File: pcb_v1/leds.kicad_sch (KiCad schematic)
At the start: 66 parts

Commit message: Included Capacitors and JST connector in schematic. Upgraded MC to 69 pin version
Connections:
- net PWRG: now also LED21.1 (GK), LED22.1 (GK); no longer LED1.2 (RK), LED10.2 (RK), LED11.2 (RK), LED12.2 (RK), LED13.2 (RK), LED14.2 (RK), LED15.2 (RK), LED17.2 (RK), LED18.2 (RK), LED19.2 (RK), LED2.2 (RK), LED20.2 (RK), LED21.2 (RK), LED22.2 (RK), LED23.2 (RK), LED24.2 (RK), LED25.2 (RK), LED26.2 (RK), LED27.2 (RK), LED28.2 (RK), LED29.2 (RK), LED30.2 (RK), LED31.2 (RK), LED32.2 (RK), LED33.2 (RK), LED34.2 (RK), LED35.2 (RK), LED36.2 (RK), LED37.2 (RK), LED38.2 (RK), LED39.2 (RK), LED40.2 (RK), LED41.2 (RK), LED42.2 (RK), LED43.2 (RK), LED44.2 (RK), LED45.2 (RK), LED46.2 (RK), LED47.2 (RK), LED48.2 (RK), LED49.2 (RK), LED5.2 (RK), LED50.2 (RK), LED51.2 (RK), LED52.2 (RK), LED53.2 (RK), LED54.2 (RK), LED55.2 (RK), LED56.2 (RK), LED57.2 (RK), LED58.2 (RK), LED59.2 (RK), LED6.2 (RK), LED60.2 (RK), LED62.2 (RK), LED64.2 (RK), LED65.2 (RK), LED66.2 (RK), LED7.2 (RK), LED8.2 (RK), LED9.2 (RK)
- net PWRR: now reaches LED3.2 (RK)
- net PWRR: now also LED1.2 (RK), LED10.2 (RK), LED11.2 (RK), LED12.2 (RK), LED13.2 (RK), LED14.2 (RK), LED15.2 (RK), LED16.2 (RK), LED17.2 (RK), LED18.2 (RK), LED19.2 (RK), LED2.2 (RK), LED20.2 (RK), LED21.2 (RK), LED22.2 (RK), LED23.2 (RK), LED24.2 (RK), LED25.2 (RK), LED26.2 (RK), LED27.2 (RK), LED28.2 (RK), LED29.2 (RK), LED30.2 (RK), LED31.2 (RK), LED32.2 (RK), LED33.2 (RK), LED34.2 (RK), LED35.2 (RK), LED36.2 (RK), LED37.2 (RK), LED38.2 (RK), LED39.2 (RK), LED4.2 (RK), LED40.2 (RK), LED41.2 (RK), LED42.2 (RK), LED43.2 (RK), LED44.2 (RK), LED45.2 (RK), LED46.2 (RK), LED47.2 (RK), LED48.2 (RK), LED49.2 (RK), LED5.2 (RK), LED50.2 (RK), LED51.2 (RK), LED52.2 (RK), LED53.2 (RK), LED54.2 (RK), LED55.2 (RK), LED56.2 (RK), LED57.2 (RK), LED58.2 (RK), LED59.2 (RK), LED6.2 (RK), LED60.2 (RK), LED61.2 (RK), LED62.2 (RK), LED64.2 (RK), LED65.2 (RK), LED66.2 (RK), LED7.2 (RK), LED8.2 (RK), LED9.2 (RK)

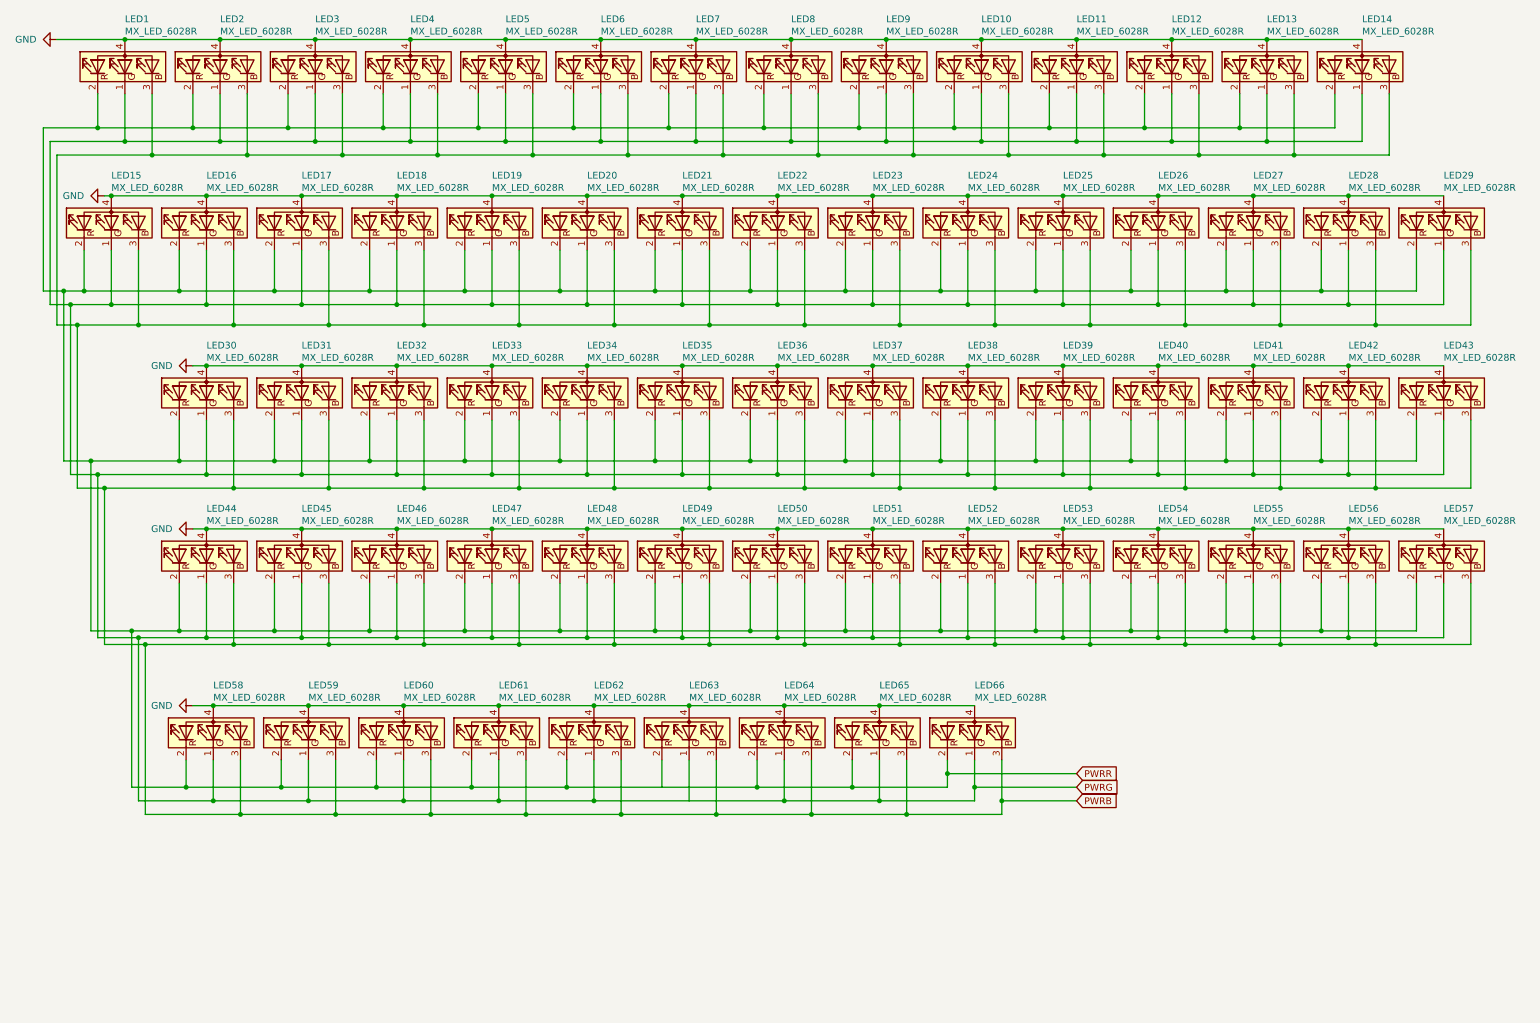
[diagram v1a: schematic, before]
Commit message: New LED Schematic
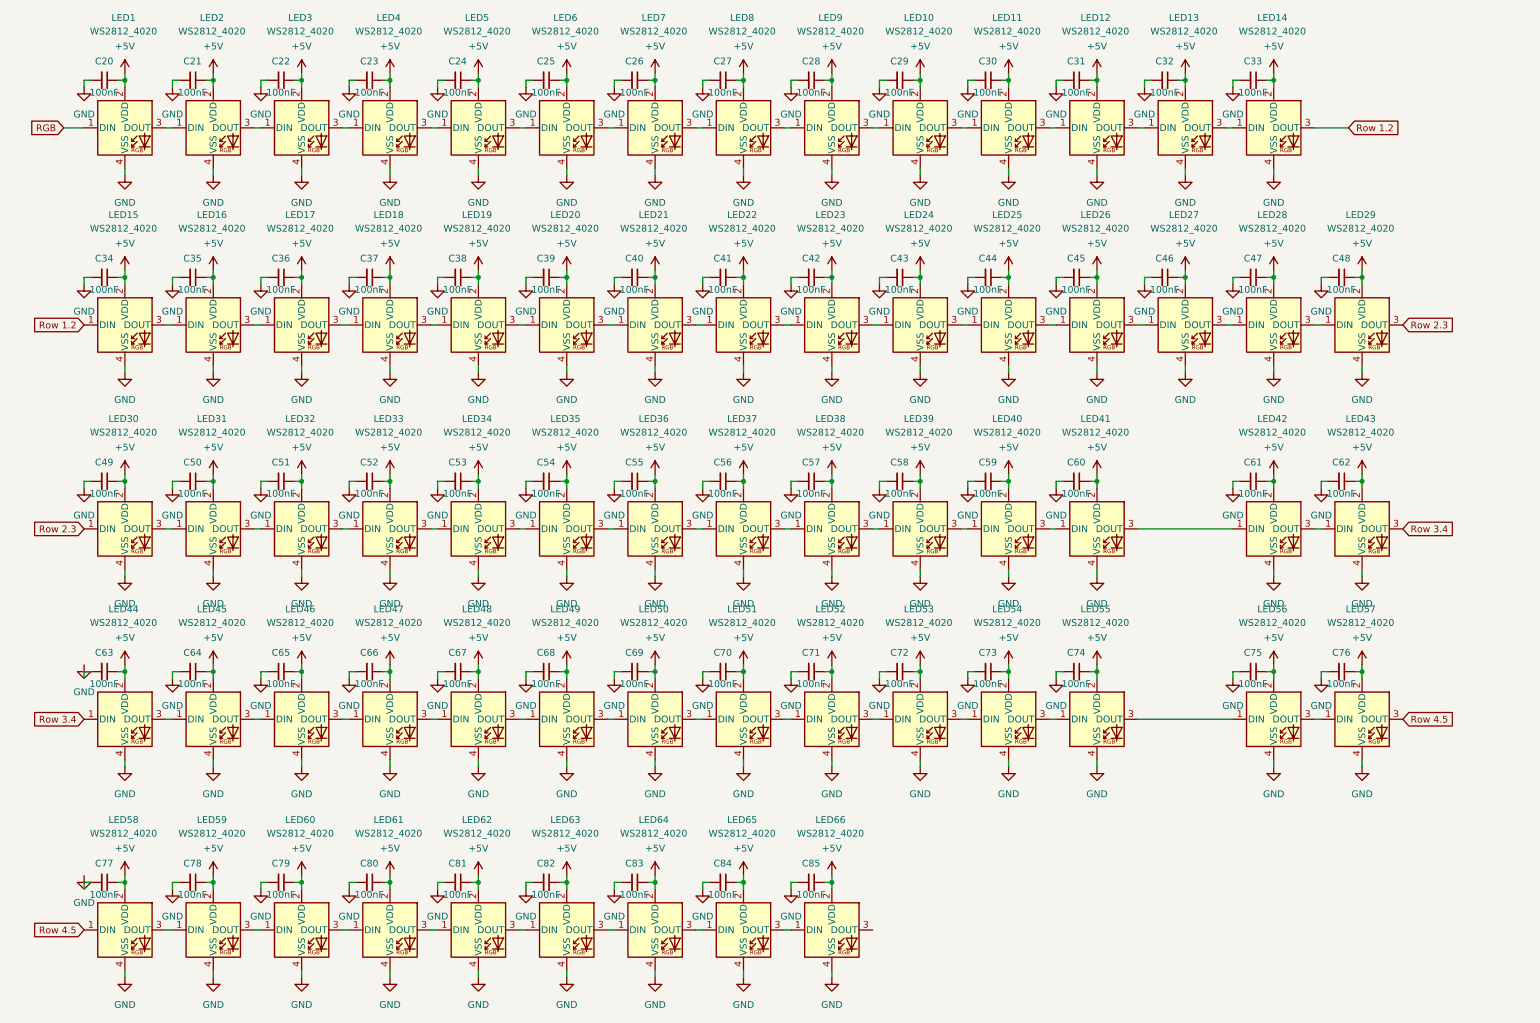
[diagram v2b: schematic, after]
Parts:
- removed LED1, LED10, LED11, LED12, LED13, LED14, LED15, LED16, LED17, LED18, LED19, LED2, LED20, LED21, LED22, LED23, LED24, LED25, LED26, LED27, LED28, LED29, LED3, LED30, LED31, LED32, LED33, LED34, LED35, LED36, LED37, LED38, LED39, LED4, LED40, LED41, LED42, LED43, LED44, LED45, LED46, LED47, LED48, LED49, LED5, LED50, LED51, LED52, LED53, LED54, LED55, LED56, LED57, LED58, LED59, LED6, LED60, LED61, LED62, LED63, LED64, LED65, LED66, LED7, LED8, LED9: MX_LED_6028R, PCM_marbastlib-mx:LED_MX_6028R, symbol PCM_marbastlib-mx:MX_LED_6028R
- added C20, C21, C22, C23, C24, C25, C26, C27, C28, C29, C30, C31, C32, C33, C34, C35, C36, C37, C38, C39, C40, C41, C42, C43, C44, C45, C46, C47, C48, C49, C50, C51, C52, C53, C54, C55, C56, C57, C58, C59, C60, C61, C62, C63, C64, C65, C66, C67, C68, C69, C70, C71, C72, C73, C74, C75, C76, C77, C78, C79, C80, C81, C82, C83, C84, C85: 100nF, Capacitor_SMD:C_0805_2012Metric, symbol Device:C_Small
- added LED1, LED10, LED11, LED12, LED13, LED14, LED15, LED16, LED17, LED18, LED19, LED2, LED20, LED21, LED22, LED23, LED24, LED25, LED26, LED27, LED28, LED29, LED3, LED30, LED31, LED32, LED33, LED34, LED35, LED36, LED37, LED38, LED39, LED4, LED40, LED41, LED42, LED43, LED44, LED45, LED46, LED47, LED48, LED49, LED5, LED50, LED51, LED52, LED53, LED54, LED55, LED56, LED57, LED58, LED59, LED6, LED60, LED61, LED62, LED63, LED64, LED65, LED66, LED7, LED8, LED9: WS2812_4020, PCM_marbastlib-various:LED_WS2812_4020, symbol PCM_marbastlib-various:WS2812_4020
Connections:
- net GND: now also C20.2, C21.2, C22.2, C23.2, C24.2, C25.2, C26.2, C27.2, C28.2, C29.2, C30.2, C31.2, C32.2, C33.2, C34.2, C35.2, C36.2, C37.2, C38.2, C39.2, C40.2, C41.2, C42.2, C43.2, C44.2, C45.2, C46.2, C47.2, C48.2, C49.2, C50.2, C51.2, C52.2, C53.2, C54.2, C55.2, C56.2, C57.2, C58.2, C59.2, C60.2, C61.2, C62.2, C64.2, C65.2, C66.2, C67.2, C68.2, C69.2, C70.2, C71.2, C72.2, C73.2, C74.2, C75.2, C76.2, C78.2, C79.2, C80.2, C81.2, C82.2, C83.2, C84.2, C85.2, LED1.4 (VSS), LED10.4 (VSS), LED11.4 (VSS), LED12.4 (VSS), LED13.4 (VSS), LED14.4 (VSS), LED15.4 (VSS), LED16.4 (VSS), LED17.4 (VSS), LED18.4 (VSS), LED19.4 (VSS), LED2.4 (VSS), LED20.4 (VSS), LED21.4 (VSS), LED22.4 (VSS), LED23.4 (VSS), LED24.4 (VSS), LED25.4 (VSS), LED26.4 (VSS), LED27.4 (VSS), LED28.4 (VSS), LED29.4 (VSS), LED3.4 (VSS), LED30.4 (VSS), LED31.4 (VSS), LED32.4 (VSS), LED33.4 (VSS), LED34.4 (VSS), LED35.4 (VSS), LED36.4 (VSS), LED37.4 (VSS), LED38.4 (VSS), LED39.4 (VSS), LED4.4 (VSS), LED40.4 (VSS), LED41.4 (VSS), LED42.4 (VSS), LED43.4 (VSS), LED44.4 (VSS), LED45.4 (VSS), LED46.4 (VSS), LED47.4 (VSS), LED48.4 (VSS), LED49.4 (VSS), LED5.4 (VSS), LED50.4 (VSS), LED51.4 (VSS), LED52.4 (VSS), LED53.4 (VSS), LED54.4 (VSS), LED55.4 (VSS), LED56.4 (VSS), LED57.4 (VSS), LED58.4 (VSS), LED59.4 (VSS), LED6.4 (VSS), LED60.4 (VSS), LED61.4 (VSS), LED62.4 (VSS), LED63.4 (VSS), LED64.4 (VSS), LED65.4 (VSS), LED66.4 (VSS), LED7.4 (VSS), LED8.4 (VSS), LED9.4 (VSS)
- new net: LED1.3 (DOUT), LED2.1 (DIN)
- new net: LED2.3 (DOUT), LED3.1 (DIN)
- new net: LED41.3 (DOUT), LED42.1 (DIN)
- new net: LED42.3 (DOUT), LED43.1 (DIN)
- new net: LED24.3 (DOUT), LED25.1 (DIN)
- new net: LED25.3 (DOUT), LED26.1 (DIN)
- new net: LED21.3 (DOUT), LED22.1 (DIN)
- new net: LED22.3 (DOUT), LED23.1 (DIN)
- new net: LED31.3 (DOUT), LED32.1 (DIN)
- new net: LED32.3 (DOUT), LED33.1 (DIN)
- new net: LED15.3 (DOUT), LED16.1 (DIN)
- new net: LED60.3 (DOUT), LED61.1 (DIN)
- new net: LED61.3 (DOUT), LED62.1 (DIN)
- new net: LED27.3 (DOUT), LED28.1 (DIN)
- new net: LED28.3 (DOUT), LED29.1 (DIN)
- new net: LED49.3 (DOUT), LED50.1 (DIN)
- new net: LED50.3 (DOUT), LED51.1 (DIN)
- new net: LED4.3 (DOUT), LED5.1 (DIN)
- new net: LED5.3 (DOUT), LED6.1 (DIN)
- new net: LED23.3 (DOUT), LED24.1 (DIN)
- new net: LED8.3 (DOUT), LED9.1 (DIN)
- new net: LED10.1 (DIN), LED9.3 (DOUT)
- new net: LED26.3 (DOUT), LED27.1 (DIN)
- new net: LED36.3 (DOUT), LED37.1 (DIN)
- new net: LED37.3 (DOUT), LED38.1 (DIN)
- new net: LED54.3 (DOUT), LED55.1 (DIN)
- new net: LED55.3 (DOUT), LED56.1 (DIN)
- new net: LED16.3 (DOUT), LED17.1 (DIN)
- new net: LED17.3 (DOUT), LED18.1 (DIN)
- new net: LED33.3 (DOUT), LED34.1 (DIN)
- new net: LED34.3 (DOUT), LED35.1 (DIN)
- new net: LED12.3 (DOUT), LED13.1 (DIN)
- new net: LED13.3 (DOUT), LED14.1 (DIN)
- new net: LED3.3 (DOUT), LED4.1 (DIN)
- new net: LED59.3 (DOUT), LED60.1 (DIN)
- new net: LED39.3 (DOUT), LED40.1 (DIN)
- new net: LED40.3 (DOUT), LED41.1 (DIN)
- new net: LED51.3 (DOUT), LED52.1 (DIN)
- new net: LED30.3 (DOUT), LED31.1 (DIN)
- new net: LED6.3 (DOUT), LED7.1 (DIN)
- new net: LED10.3 (DOUT), LED11.1 (DIN)
- new net: LED19.3 (DOUT), LED20.1 (DIN)
- new net: LED20.3 (DOUT), LED21.1 (DIN)
- new net: LED65.3 (DOUT), LED66.1 (DIN)
- new net: LED38.3 (DOUT), LED39.1 (DIN)
- new net: LED56.3 (DOUT), LED57.1 (DIN)
- new net: LED46.3 (DOUT), LED47.1 (DIN)
- new net: LED47.3 (DOUT), LED48.1 (DIN)
- new net: LED48.3 (DOUT), LED49.1 (DIN)
- new net: LED11.3 (DOUT), LED12.1 (DIN)
- new net: LED18.3 (DOUT), LED19.1 (DIN)
- new net: LED44.3 (DOUT), LED45.1 (DIN)
- new net: LED45.3 (DOUT), LED46.1 (DIN)
- new net: LED35.3 (DOUT), LED36.1 (DIN)
- new net: LED63.3 (DOUT), LED64.1 (DIN)
- new net: LED64.3 (DOUT), LED65.1 (DIN)
- new net: LED53.3 (DOUT), LED54.1 (DIN)
- new net: LED62.3 (DOUT), LED63.1 (DIN)
- new net: LED7.3 (DOUT), LED8.1 (DIN)
- new net: LED58.3 (DOUT), LED59.1 (DIN)
- new net: LED52.3 (DOUT), LED53.1 (DIN)
- new net +5V: C20.1, C21.1, C22.1, C23.1, C24.1, C25.1, C26.1, C27.1, C28.1, C29.1, C30.1, C31.1, C32.1, C33.1, C34.1, C35.1, C36.1, C37.1, C38.1, C39.1, C40.1, C41.1, C42.1, C43.1, C44.1, C45.1, C46.1, C47.1, C48.1, C49.1, C50.1, C51.1, C52.1, C53.1, C54.1, C55.1, C56.1, C57.1, C58.1, C59.1, C60.1, C61.1, C62.1, C63.1, C64.1, C65.1, C66.1, C67.1, C68.1, C69.1, C70.1, C71.1, C72.1, C73.1, C74.1, C75.1, C76.1, C77.1, C78.1, C79.1, C80.1, C81.1, C82.1, C83.1, C84.1, C85.1, LED1.2 (VDD), LED10.2 (VDD), LED11.2 (VDD), LED12.2 (VDD), LED13.2 (VDD), LED14.2 (VDD), LED15.2 (VDD), LED16.2 (VDD), LED17.2 (VDD), LED18.2 (VDD), LED19.2 (VDD), LED2.2 (VDD), LED20.2 (VDD), LED21.2 (VDD), LED22.2 (VDD), LED23.2 (VDD), LED24.2 (VDD), LED25.2 (VDD), LED26.2 (VDD), LED27.2 (VDD), LED28.2 (VDD), LED29.2 (VDD), LED3.2 (VDD), LED30.2 (VDD), LED31.2 (VDD), LED32.2 (VDD), LED33.2 (VDD), LED34.2 (VDD), LED35.2 (VDD), LED36.2 (VDD), LED37.2 (VDD), LED38.2 (VDD), LED39.2 (VDD), LED4.2 (VDD), LED40.2 (VDD), LED41.2 (VDD), LED42.2 (VDD), LED43.2 (VDD), LED44.2 (VDD), LED45.2 (VDD), LED46.2 (VDD), LED47.2 (VDD), LED48.2 (VDD), LED49.2 (VDD), LED5.2 (VDD), LED50.2 (VDD), LED51.2 (VDD), LED52.2 (VDD), LED53.2 (VDD), LED54.2 (VDD), LED55.2 (VDD), LED56.2 (VDD), LED57.2 (VDD), LED58.2 (VDD), LED59.2 (VDD), LED6.2 (VDD), LED60.2 (VDD), LED61.2 (VDD), LED62.2 (VDD), LED63.2 (VDD), LED64.2 (VDD), LED65.2 (VDD), LED66.2 (VDD), LED7.2 (VDD), LED8.2 (VDD), LED9.2 (VDD)
- new net RGB: LED1.1 (DIN)
- new net Row 1.2: LED14.3 (DOUT), LED15.1 (DIN)
- new net Row 2.3: LED29.3 (DOUT), LED30.1 (DIN)
- new net Row 3.4: LED43.3 (DOUT), LED44.1 (DIN)
- new net Row 4.5: LED57.3 (DOUT), LED58.1 (DIN)

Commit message: Replaced and wired LEDs and Capacitors
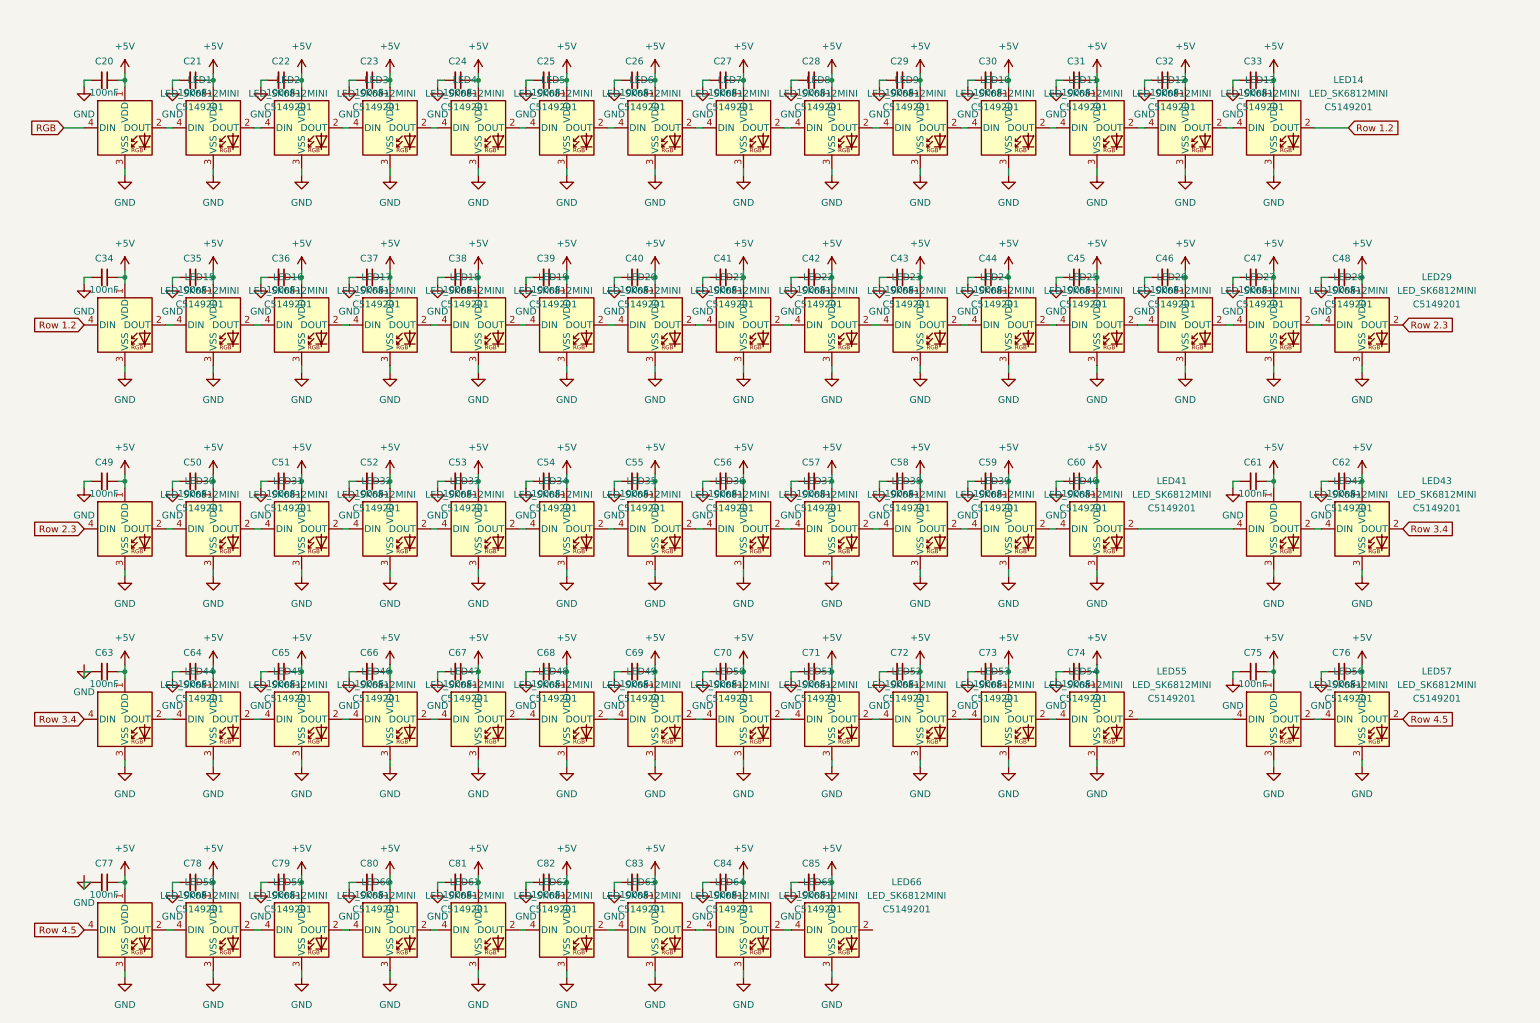
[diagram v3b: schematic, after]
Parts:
- removed LED1, LED10, LED11, LED12, LED13, LED14, LED15, LED16, LED17, LED18, LED19, LED2, LED20, LED21, LED22, LED23, LED24, LED25, LED26, LED27, LED28, LED29, LED3, LED30, LED31, LED32, LED33, LED34, LED35, LED36, LED37, LED38, LED39, LED4, LED40, LED41, LED42, LED43, LED44, LED45, LED46, LED47, LED48, LED49, LED5, LED50, LED51, LED52, LED53, LED54, LED55, LED56, LED57, LED58, LED59, LED6, LED60, LED61, LED62, LED63, LED64, LED65, LED66, LED7, LED8, LED9: WS2812_4020, PCM_marbastlib-various:LED_WS2812_4020, symbol PCM_marbastlib-various:WS2812_4020
- added LED1, LED10, LED11, LED12, LED13, LED14, LED15, LED16, LED17, LED18, LED19, LED2, LED20, LED21, LED22, LED23, LED24, LED25, LED26, LED27, LED28, LED29, LED3, LED30, LED31, LED32, LED33, LED34, LED35, LED36, LED37, LED38, LED39, LED4, LED40, LED41, LED42, LED43, LED44, LED45, LED46, LED47, LED48, LED49, LED5, LED50, LED51, LED52, LED53, LED54, LED55, LED56, LED57, LED58, LED59, LED6, LED60, LED61, LED62, LED63, LED64, LED65, LED66, LED7, LED8, LED9: LED_SK6812MINI, ScottoKeebs_Components:LED_SK6812MINI, symbol ScottoKeebs:LED_SK6812MINI
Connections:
- net +5V: now also LED1.1 (VDD), LED10.1 (VDD), LED11.1 (VDD), LED12.1 (VDD), LED13.1 (VDD), LED14.1 (VDD), LED15.1 (VDD), LED16.1 (VDD), LED17.1 (VDD), LED18.1 (VDD), LED19.1 (VDD), LED2.1 (VDD), LED20.1 (VDD), LED21.1 (VDD), LED22.1 (VDD), LED23.1 (VDD), LED24.1 (VDD), LED25.1 (VDD), LED26.1 (VDD), LED27.1 (VDD), LED28.1 (VDD), LED29.1 (VDD), LED3.1 (VDD), LED30.1 (VDD), LED31.1 (VDD), LED32.1 (VDD), LED33.1 (VDD), LED34.1 (VDD), LED35.1 (VDD), LED36.1 (VDD), LED37.1 (VDD), LED38.1 (VDD), LED39.1 (VDD), LED4.1 (VDD), LED40.1 (VDD), LED41.1 (VDD), LED42.1 (VDD), LED43.1 (VDD), LED44.1 (VDD), LED45.1 (VDD), LED46.1 (VDD), LED47.1 (VDD), LED48.1 (VDD), LED49.1 (VDD), LED5.1 (VDD), LED50.1 (VDD), LED51.1 (VDD), LED52.1 (VDD), LED53.1 (VDD), LED54.1 (VDD), LED55.1 (VDD), LED56.1 (VDD), LED57.1 (VDD), LED58.1 (VDD), LED59.1 (VDD), LED6.1 (VDD), LED60.1 (VDD), LED61.1 (VDD), LED62.1 (VDD), LED63.1 (VDD), LED64.1 (VDD), LED65.1 (VDD), LED66.1 (VDD), LED7.1 (VDD), LED8.1 (VDD), LED9.1 (VDD)
- net GND: now also LED1.3 (VSS), LED10.3 (VSS), LED11.3 (VSS), LED12.3 (VSS), LED13.3 (VSS), LED14.3 (VSS), LED15.3 (VSS), LED16.3 (VSS), LED17.3 (VSS), LED18.3 (VSS), LED19.3 (VSS), LED2.3 (VSS), LED20.3 (VSS), LED21.3 (VSS), LED22.3 (VSS), LED23.3 (VSS), LED24.3 (VSS), LED25.3 (VSS), LED26.3 (VSS), LED27.3 (VSS), LED28.3 (VSS), LED29.3 (VSS), LED3.3 (VSS), LED30.3 (VSS), LED31.3 (VSS), LED32.3 (VSS), LED33.3 (VSS), LED34.3 (VSS), LED35.3 (VSS), LED36.3 (VSS), LED37.3 (VSS), LED38.3 (VSS), LED39.3 (VSS), LED4.3 (VSS), LED40.3 (VSS), LED41.3 (VSS), LED42.3 (VSS), LED43.3 (VSS), LED44.3 (VSS), LED45.3 (VSS), LED46.3 (VSS), LED47.3 (VSS), LED48.3 (VSS), LED49.3 (VSS), LED5.3 (VSS), LED50.3 (VSS), LED51.3 (VSS), LED52.3 (VSS), LED53.3 (VSS), LED54.3 (VSS), LED55.3 (VSS), LED56.3 (VSS), LED57.3 (VSS), LED58.3 (VSS), LED59.3 (VSS), LED6.3 (VSS), LED60.3 (VSS), LED61.3 (VSS), LED62.3 (VSS), LED63.3 (VSS), LED64.3 (VSS), LED65.3 (VSS), LED66.3 (VSS), LED7.3 (VSS), LED8.3 (VSS), LED9.3 (VSS)
- net RGB: now also LED1.4 (DIN)
- net Row 1.2: now also LED14.2 (DOUT), LED15.4 (DIN)
- net Row 2.3: now also LED29.2 (DOUT), LED30.4 (DIN)
- net Row 3.4: now also LED43.2 (DOUT), LED44.4 (DIN)
- net Row 4.5: now also LED57.2 (DOUT), LED58.4 (DIN)
- new net: LED10.4 (DIN), LED9.2 (DOUT)
- new net: LED8.2 (DOUT), LED9.4 (DIN)
- new net: LED42.2 (DOUT), LED43.4 (DIN)
- new net: LED52.2 (DOUT), LED53.4 (DIN)
- new net: LED51.2 (DOUT), LED52.4 (DIN)
- new net: LED19.2 (DOUT), LED20.4 (DIN)
- new net: LED18.2 (DOUT), LED19.4 (DIN)
- new net: LED60.2 (DOUT), LED61.4 (DIN)
- new net: LED59.2 (DOUT), LED60.4 (DIN)
- new net: LED16.2 (DOUT), LED17.4 (DIN)
- new net: LED15.2 (DOUT), LED16.4 (DIN)
- new net: LED3.2 (DOUT), LED4.4 (DIN)
- new net: LED2.2 (DOUT), LED3.4 (DIN)
- new net: LED61.2 (DOUT), LED62.4 (DIN)
- new net: LED65.2 (DOUT), LED66.4 (DIN)
- new net: LED22.2 (DOUT), LED23.4 (DIN)
- new net: LED21.2 (DOUT), LED22.4 (DIN)
- new net: LED50.2 (DOUT), LED51.4 (DIN)
- new net: LED49.2 (DOUT), LED50.4 (DIN)
- new net: LED27.2 (DOUT), LED28.4 (DIN)
- new net: LED26.2 (DOUT), LED27.4 (DIN)
- new net: LED34.2 (DOUT), LED35.4 (DIN)
- new net: LED33.2 (DOUT), LED34.4 (DIN)
- new net: LED64.2 (DOUT), LED65.4 (DIN)
- new net: LED63.2 (DOUT), LED64.4 (DIN)
- new net: LED28.2 (DOUT), LED29.4 (DIN)
- new net: LED7.2 (DOUT), LED8.4 (DIN)
- new net: LED6.2 (DOUT), LED7.4 (DIN)
- new net: LED5.2 (DOUT), LED6.4 (DIN)
- new net: LED4.2 (DOUT), LED5.4 (DIN)
- new net: LED38.2 (DOUT), LED39.4 (DIN)
- new net: LED37.2 (DOUT), LED38.4 (DIN)
- new net: LED1.2 (DOUT), LED2.4 (DIN)
- new net: LED13.2 (DOUT), LED14.4 (DIN)
- new net: LED12.2 (DOUT), LED13.4 (DIN)
- new net: LED58.2 (DOUT), LED59.4 (DIN)
- new net: LED45.2 (DOUT), LED46.4 (DIN)
- new net: LED44.2 (DOUT), LED45.4 (DIN)
- new net: LED25.2 (DOUT), LED26.4 (DIN)
- new net: LED24.2 (DOUT), LED25.4 (DIN)
- new net: LED56.2 (DOUT), LED57.4 (DIN)
- new net: LED55.2 (DOUT), LED56.4 (DIN)
- new net: LED54.2 (DOUT), LED55.4 (DIN)
- new net: LED53.2 (DOUT), LED54.4 (DIN)
- new net: LED40.2 (DOUT), LED41.4 (DIN)
- new net: LED39.2 (DOUT), LED40.4 (DIN)
- new net: LED17.2 (DOUT), LED18.4 (DIN)
- new net: LED31.2 (DOUT), LED32.4 (DIN)
- new net: LED30.2 (DOUT), LED31.4 (DIN)
- new net: LED48.2 (DOUT), LED49.4 (DIN)
- new net: LED36.2 (DOUT), LED37.4 (DIN)
- new net: LED11.2 (DOUT), LED12.4 (DIN)
- new net: LED47.2 (DOUT), LED48.4 (DIN)
- new net: LED23.2 (DOUT), LED24.4 (DIN)
- new net: LED35.2 (DOUT), LED36.4 (DIN)
- new net: LED46.2 (DOUT), LED47.4 (DIN)
- new net: LED62.2 (DOUT), LED63.4 (DIN)
- new net: LED20.2 (DOUT), LED21.4 (DIN)
- new net: LED41.2 (DOUT), LED42.4 (DIN)
- new net: LED32.2 (DOUT), LED33.4 (DIN)
- new net: LED10.2 (DOUT), LED11.4 (DIN)

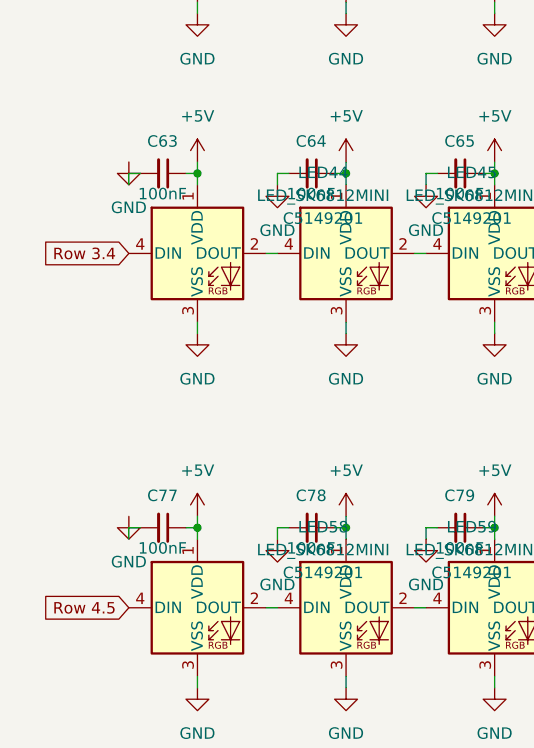
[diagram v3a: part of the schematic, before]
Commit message: Fixed Via Sizes
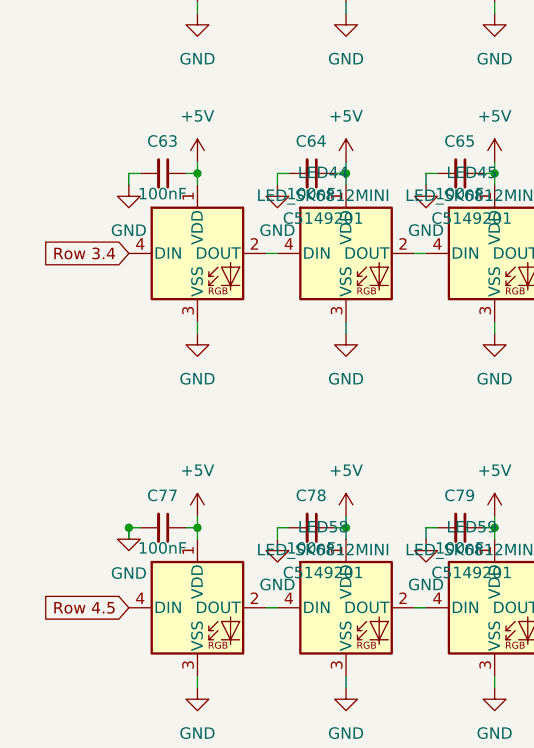
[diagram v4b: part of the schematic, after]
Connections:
- net GND: now also C63.2, C77.2
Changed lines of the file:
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@@
 	)
 	(junction
+		(at 22.86 177.8)
+		(diameter 0)
+		(color 0 0 0 0)
+	)
+	(junction
 		(at 113.03 102.87)
 		(diameter 0)
@@
 	(symbol
 		(lib_id "power:GND")
-		(at 22.86 176.53 0)
+		(at 22.86 177.8 0)
 		(mirror y)
 		(unit 1)
@@
 		(dnp no)
 		(property "Reference" "#PWR0137"
-			(at 22.86 182.88 0)
+			(at 22.86 184.15 0)
 			(effects
 				(font
@@
 		)
 		(property "Value" "GND"
-			(at 22.86 181.61 0)
+			(at 22.86 182.88 0)
 			(effects
 				(font
@@
 		)
 		(property "Footprint" ""
-			(at 22.86 176.53 0)
+			(at 22.86 177.8 0)
 			(effects
 				(font
@@
 		)
 		(property "Datasheet" ""
-			(at 22.86 176.53 0)
+			(at 22.86 177.8 0)
 			(effects
 				(font
@@
 		)
 		(property "Description" "Power symbol creates a global label with name \"GND\" , ground"
-			(at 22.86 176.53 0)
+			(at 22.86 177.8 0)
 			(effects
 				(font
@@
 	(symbol
 		(lib_id "power:GND")
-		(at 22.86 137.16 0)
+		(at 22.86 139.7 0)
 		(mirror y)
 		(unit 1)
@@
 		(dnp no)
 		(property "Reference" "#PWR0109"
-			(at 22.86 143.51 0)
+			(at 22.86 146.05 0)
 			(effects
 				(font
@@
 		)
 		(property "Value" "GND"
-			(at 22.86 142.24 0)
+			(at 22.86 144.78 0)
 			(effects
 				(font
@@
 		)
 		(property "Footprint" ""
-			(at 22.86 137.16 0)
+			(at 22.86 139.7 0)
 			(effects
 				(font
@@
 		)
 		(property "Datasheet" ""
-			(at 22.86 137.16 0)
+			(at 22.86 139.7 0)
 			(effects
 				(font
@@
 		)
 		(property "Description" "Power symbol creates a global label with name \"GND\" , ground"
-			(at 22.86 137.16 0)
+			(at 22.86 139.7 0)
 			(effects
 				(font
